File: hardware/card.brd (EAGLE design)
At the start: 97 x 56 mm, 93 parts, among them J1 UE27AC54100, J2 MICROSD, J3 0541323062, J4 6-PIN_2MM-V, J5 JST_2PIN, J6 B2PS-VH(LF)(SN), J7 MINI-USB-UX60A-MB-5ST, J8 JST_2PIN, U1 ATSAMD21J_QFN, U2 TS3USB221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

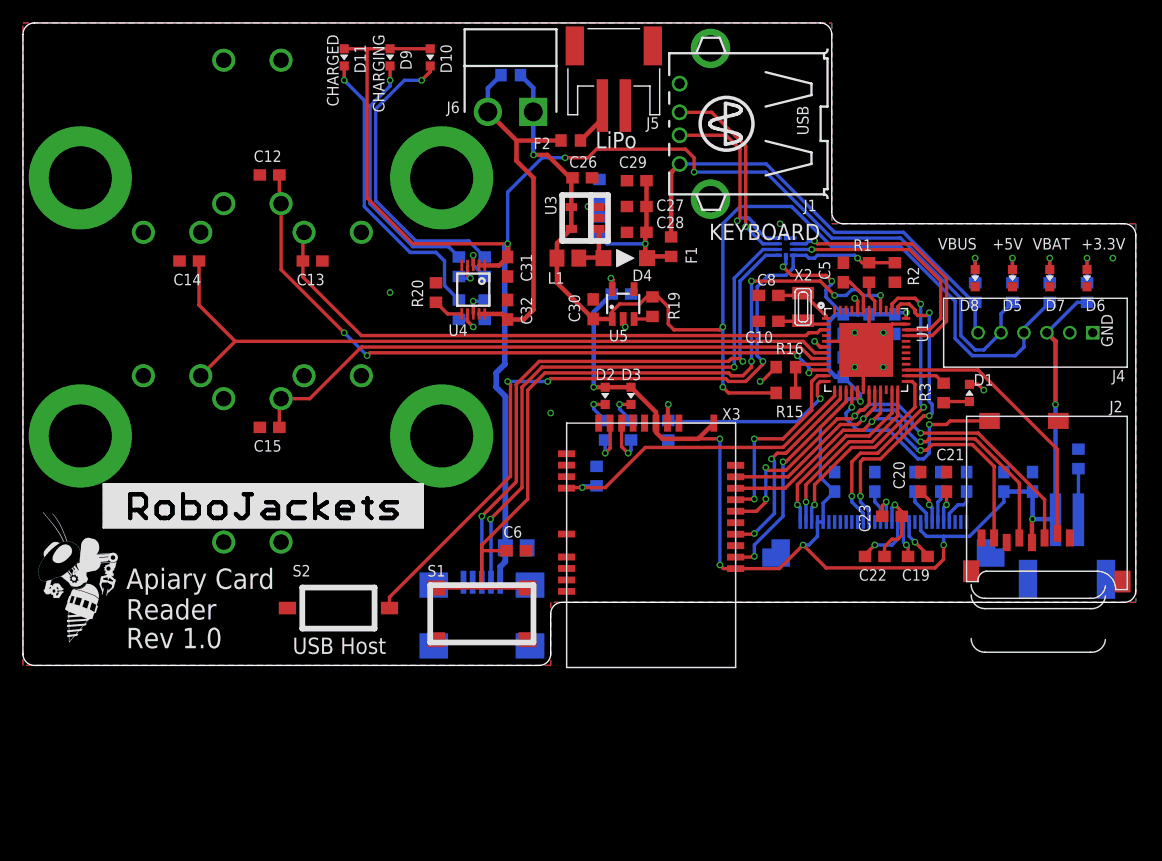
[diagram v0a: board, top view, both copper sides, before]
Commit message: Increase board size to put USB-B port at the edge of the case
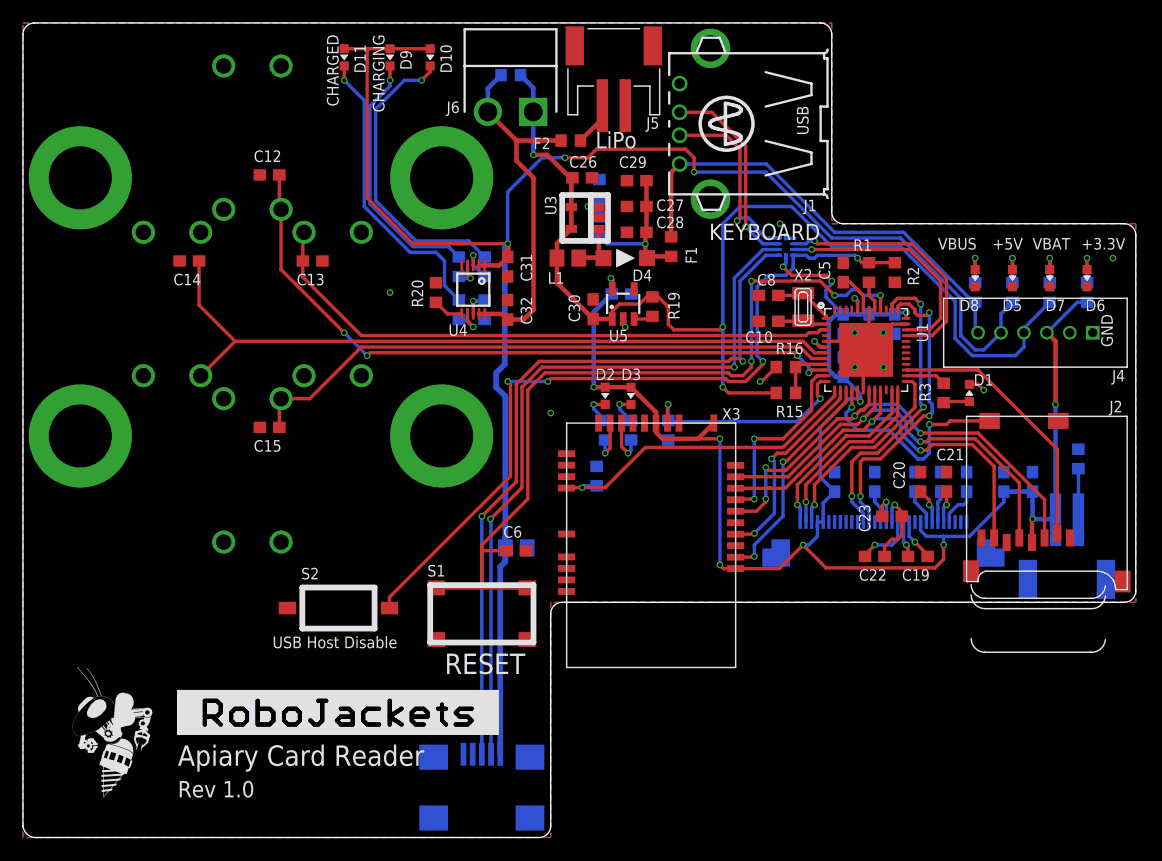
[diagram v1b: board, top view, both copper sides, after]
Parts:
- moved U$2 19.1 mm to (13.5, -6.00)
- moved J7 15.0 mm to (40.0, -10.0)
- moved U$1 13.8 mm to (7.00, -11.5)
- moved S3 0.50 mm to (20.0, 46.0)
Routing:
- net 1D-: track 50.0 -> 65.0 mm
- net +5V: track 131.4 -> 146.4 mm
- net 1D+: track 50.7 -> 65.7 mm
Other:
- board size 97 x 56 mm -> 97 x 71 mm
- board text added: "RESET"
- board text added: "USB Host Disable"
- board text removed: "USB Host"
